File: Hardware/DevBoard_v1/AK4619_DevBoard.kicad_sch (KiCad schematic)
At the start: 78 parts, among them J1 Power, J2 Power, J3 In, J4 Out, J5 Out_Amp, J6 Conn_02x08_Odd_Even, J7 Conn_02x15_Odd_Even, J8 Conn_02x10_Odd_Even, J9 Conn_02x17_Odd_Even, U1 TL074, U2 MCP6004, U3 Hyperram_BGA, U4 AK4619VN

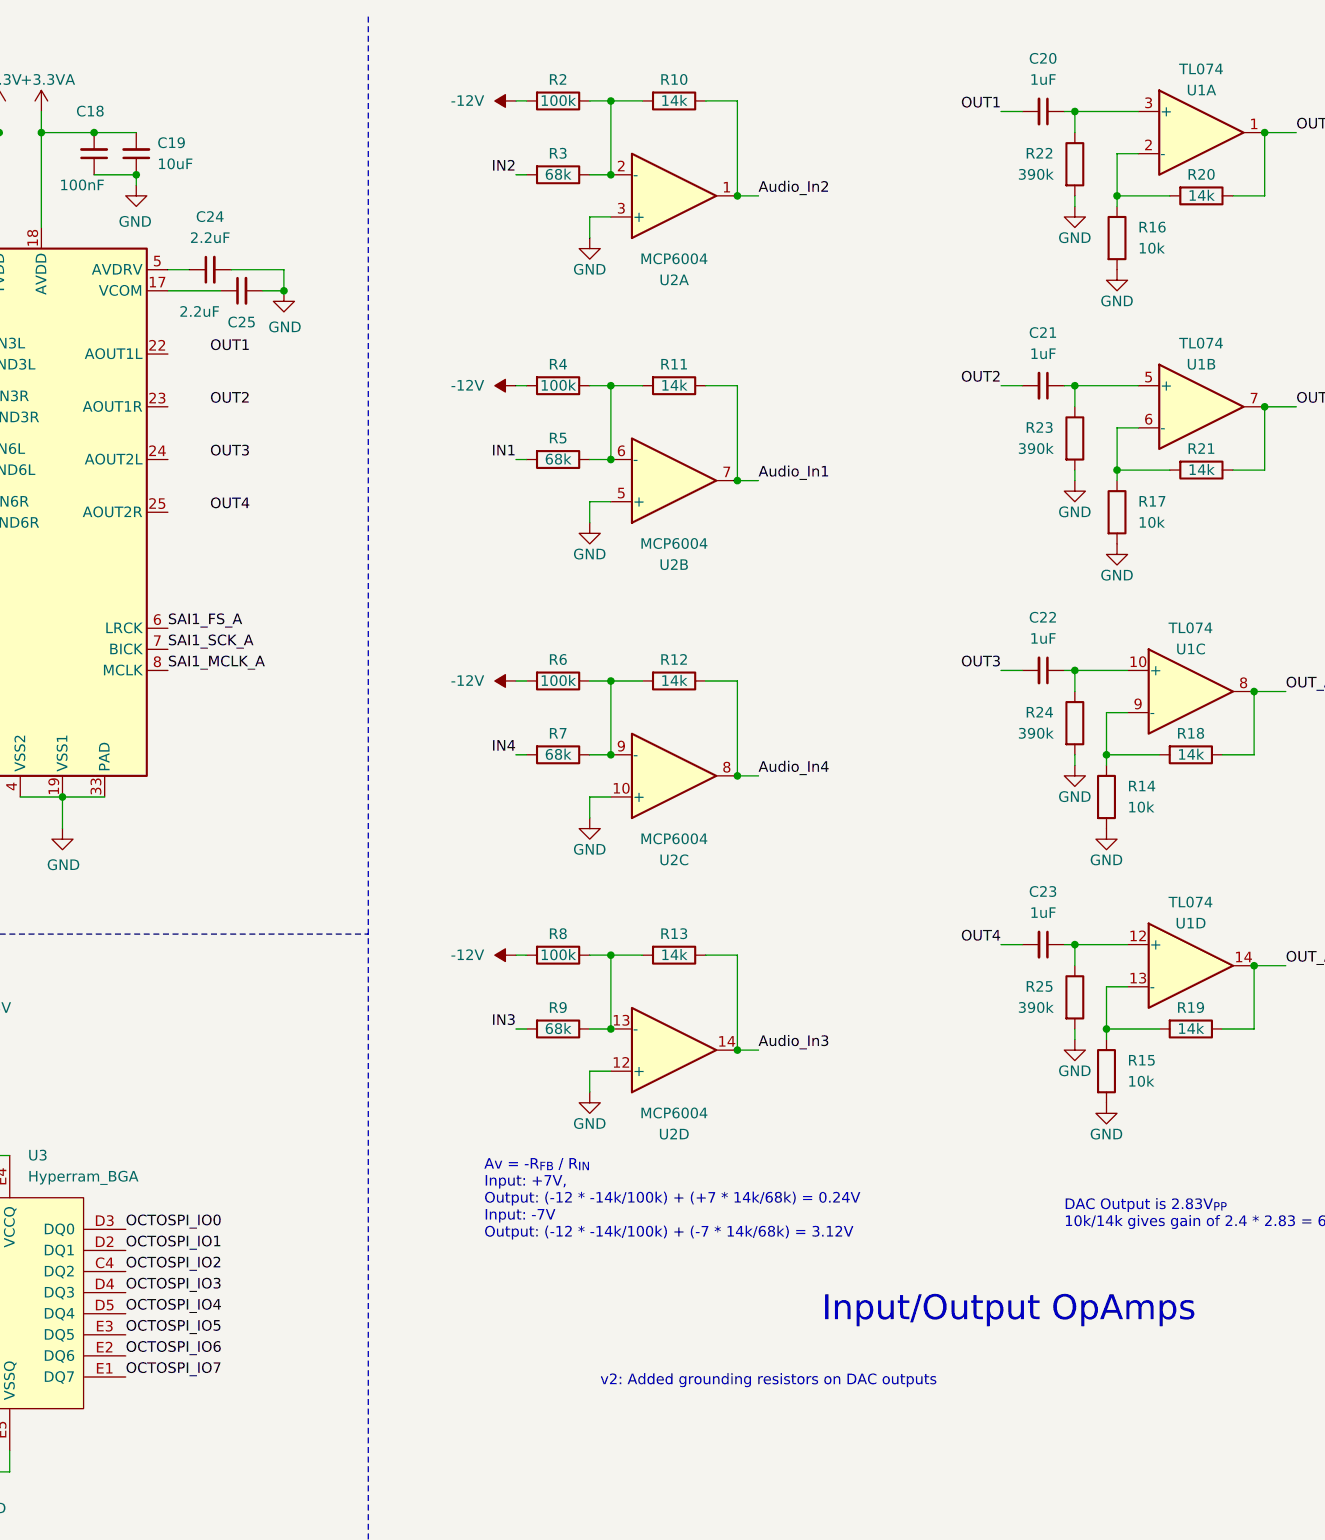
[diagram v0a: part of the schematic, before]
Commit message: Cleaned up Audio Codec test signal loop-back
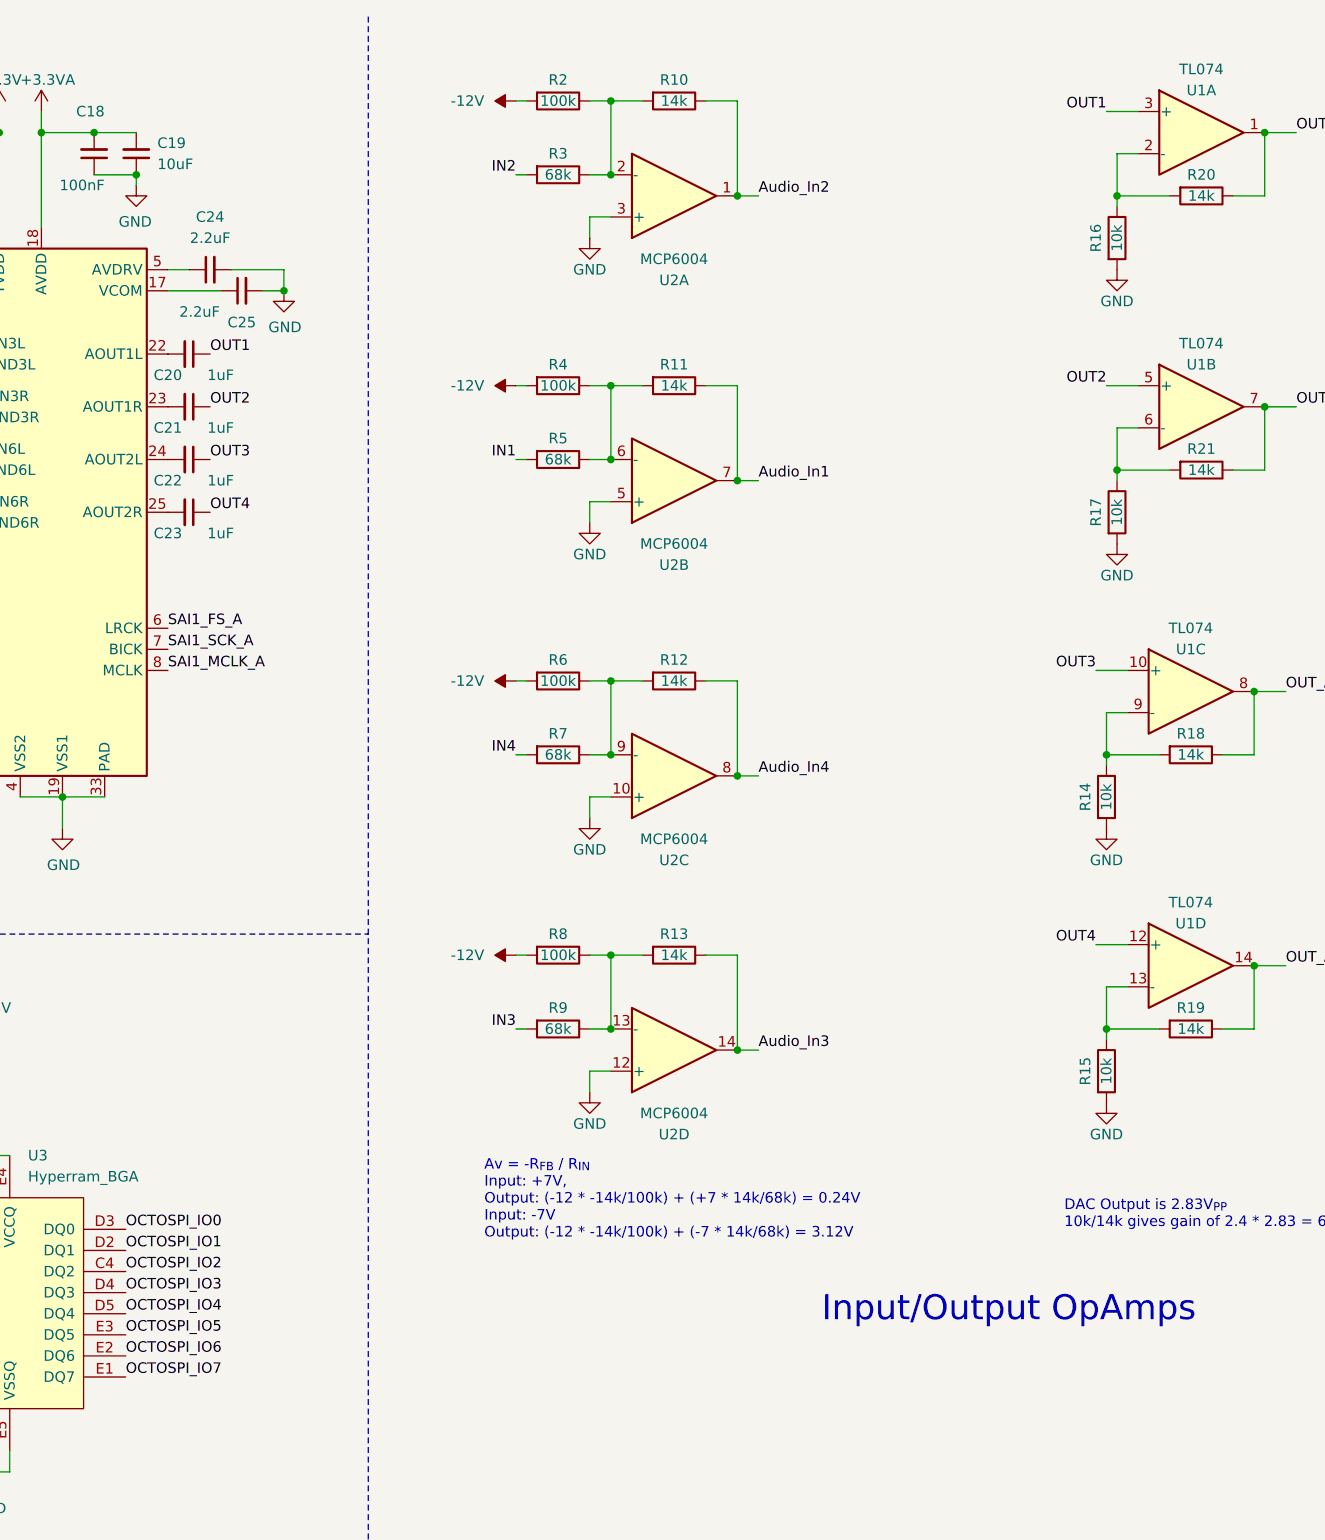
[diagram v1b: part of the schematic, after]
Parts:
- removed R22, R23, R24, R25: 390k, Resistor_SMD:R_0603_1608Metric_Pad0.98x0.95mm_HandSolder, symbol Device:R
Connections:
- net OUT1: now also C20.1, U1.3 (+); no longer C20.2
- net OUT2: now also C21.1, U1.5 (+); no longer C21.2
- net OUT3: now also C22.1, U1.10 (+); no longer C22.2
- net OUT4: now also C23.1, U1.12 (+); no longer C23.2
- net at U4.22 (AOUT1L): now also C20.2
- net at U4.23 (AOUT1R): now also C21.2
- net at U4.24 (AOUT2L): now also C22.2
- net at U4.25 (AOUT2R): now also C23.2
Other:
- note removed: "v2: Added grounding resistors on DAC outputs"
- moved on the sheet: C20, C21, C22, C23
